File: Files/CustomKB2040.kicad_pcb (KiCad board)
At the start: 2 copper layers, 3.9 x 3.6 mm, 153 parts, among them J1 USB_C_Receptacle, J3 USB_C_Receptacle, J4 USB_C_Receptacle, J5 Conn_01x03_Pin, J6 USB_C_Receptacle, U1 W25Q128JVS, U2 XC6206-3.3_SOT, U3 USBLC6-2SC6, U4 RP2040, U5 W25Q128JVS, U6 XC6206-3.3_SOT, U7 USBLC6-2SC6, U8 RP2040, Y1 Crystal_GND24, Y2 Crystal_GND24

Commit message: placed companets and semi routed
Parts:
- added REF**: MountingHole_2.2mm_M2_DIN965_Pad, MountingHole:MountingHole_2.2mm_M2_DIN965_Pad, F.Cu at (46.3, 103.3)
- added REF**: MountingHole_2.2mm_M2_DIN965_Pad, MountingHole:MountingHole_2.2mm_M2_DIN965_Pad, F.Cu at (40.4, 52.2)
- added REF**: MountingHole_2.2mm_M2_DIN965_Pad, MountingHole:MountingHole_2.2mm_M2_DIN965_Pad, F.Cu at (119.9, 98.6)
- added REF**: MountingHole_2.2mm_M2_DIN965_Pad, MountingHole:MountingHole_2.2mm_M2_DIN965_Pad, F.Cu at (138.0, 45.0)
- added REF**: MountingHole_2.2mm_M2_DIN965_Pad, MountingHole:MountingHole_2.2mm_M2_DIN965_Pad, F.Cu at (120.0, 45.0)
- added REF**: MountingHole_2.2mm_M2_DIN965_Pad, MountingHole:MountingHole_2.2mm_M2_DIN965_Pad, F.Cu at (138.9, 98.6)
- added REF**: MountingHole_2.2mm_M2_DIN965_Pad, MountingHole:MountingHole_2.2mm_M2_DIN965_Pad, F.Cu at (99.8, 61.8)
- BOOT1, D1, D2, F1, J1, J3, RESET1, U1, U2, U3, U4, Y1: moved to F.Cu
- C1, C10, C2, C3, C4, C5, C6: footprint ScottoKeebs_Components:Capacitor_0603 -> Capacitor_SMD:C_0805_2012Metric_Pad1.18x1.45mm_HandSolder; moved to F.Cu
- C11, C13, C14, C15, C16, C17, C18, C19, C20, C21, C22, C23, C24, C25, C27, C28, C29, C31, C32, C33, C34, C35, C36, C7, C9: footprint ScottoKeebs_Components:Capacitor_0603 -> Capacitor_SMD:C_0805_2012Metric_Pad1.18x1.45mm_HandSolder
- C12, C26, C30, C8: footprint ScottoKeebs_Components:Capacitor_0402 -> Capacitor_SMD:C_0805_2012Metric_Pad1.18x1.45mm_HandSolder
- R1, R10, R2, R5, R6, R7, R8, R9: footprint Resistor_SMD:R_0603_1608Metric -> Resistor_SMD:R_0805_2012Metric_Pad1.20x1.40mm_HandSolder; moved to F.Cu
- R11, R12, R13, R14, R15, R16, R17, R18, R19, R20, R3, R4: footprint Resistor_SMD:R_0603_1608Metric -> Resistor_SMD:R_0805_2012Metric_Pad1.20x1.40mm_HandSolder
- moved C26 192.8 mm to (231.0, 108.4)
- moved C30 192.8 mm to (231.0, 110.4)
- moved D3 192.8 mm to (242.5, 101.0)
- moved D37 192.8 mm to (243.8, 21.6)
- moved D38 192.8 mm to (243.8, 26.2)
- moved D39 192.8 mm to (243.8, 30.8)
- moved D4 192.8 mm to (242.5, 105.3)
- moved D40 192.8 mm to (243.8, 35.5)
- moved J5 192.8 mm to (227.8, 93.7)
- moved R15 192.8 mm to (238.4, 74.0)
- moved R16 192.8 mm to (238.4, 76.5)
- moved R17 192.8 mm to (238.4, 79.1)
- moved R18 192.8 mm to (238.4, 81.6)
- moved R19 192.8 mm to (238.4, 84.1)
- moved R20 192.8 mm to (238.4, 86.6)
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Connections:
- R10 pad 1: GPIO25 -> GPIO_19
- U4 pad 24: SWCLK -> unconnected-(U4-SWCLK-Pad24)
- U4 pad 25: SWD -> unconnected-(U4-SWD-Pad25)
- U4 pad 30: L_TX -> GPIO_19
- U4 pad 31: L_RX -> unconnected-(U4-GPIO20-Pad31)
- U4 pad 36: unconnected-(U4-GPIO24-Pad36) -> L_TX
- U4 pad 37: GPIO25 -> L_RX
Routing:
- net +5V: track 0.00 -> 445.7 mm, vias 0 -> 7
- net L_TX: track 0.00 -> 26.1 mm
- net L_RX: track 0.00 -> 25.2 mm
- net QSPI_SD3: track 0.00 -> 14.2 mm, vias 0 -> 1
- net QSPI_SCLK: track 0.00 -> 13.6 mm, vias 0 -> 2
- net +3V3: track 0.00 -> 13.5 mm, vias 0 -> 4
- net QSPI_SD0: track 0.00 -> 12.8 mm, vias 0 -> 2
- net +1V1: track 0.00 -> 9.19 mm, vias 0 -> 2
- net QSPI_SS: track 0.00 -> 7.95 mm
- net QSPI_SD1: track 0.00 -> 7.35 mm
- net QSPI_SD2: track 0.00 -> 6.43 mm
- net Net-(U4-XIN): track 0.00 -> 6.35 mm
- net Net-(U4-XOUT): track 0.00 -> 5.43 mm
- net Net-(U2-VO): track 0.00 -> 4.29 mm
- net Net-(C6-Pad1): track 0.00 -> 4.17 mm
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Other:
- board size 3.9 x 3.6 mm -> 225.2 x 105.2 mm

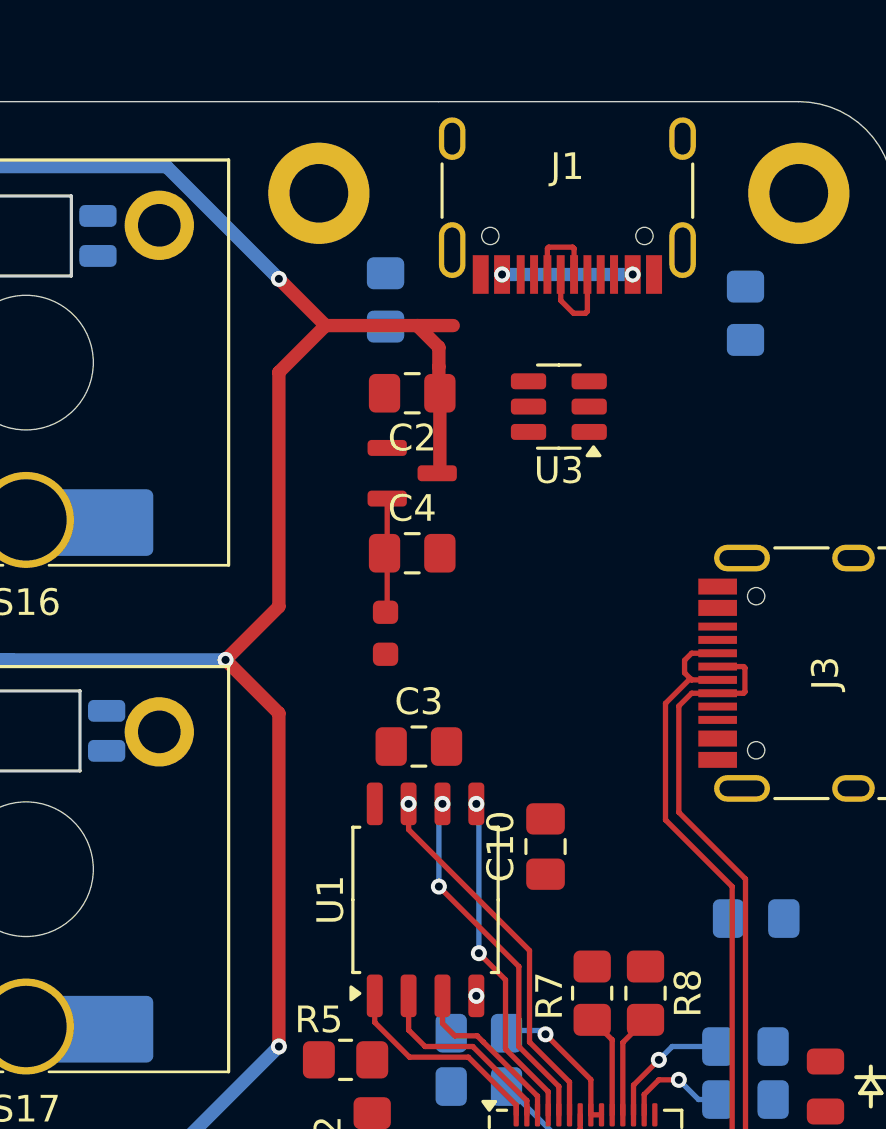
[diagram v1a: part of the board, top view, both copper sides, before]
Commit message: placed companets and semi routed
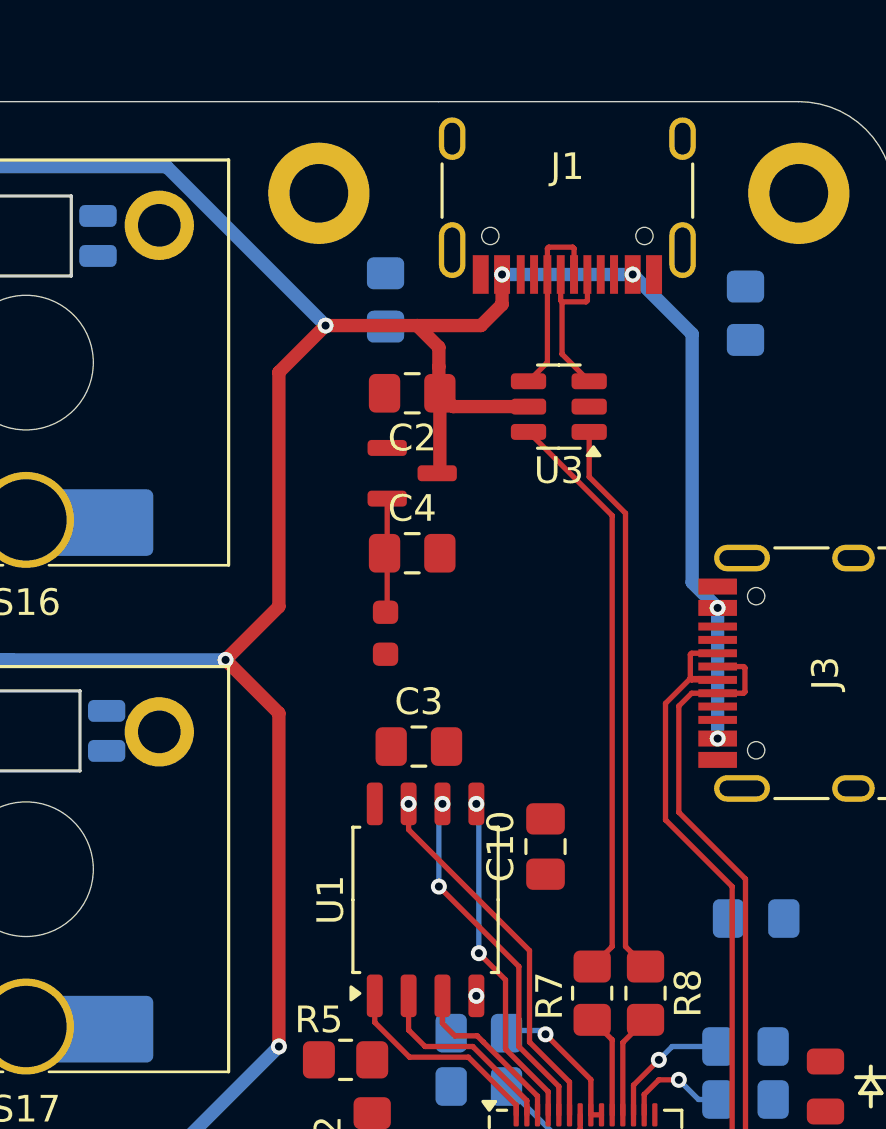
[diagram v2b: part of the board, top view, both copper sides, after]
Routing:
- net +5V: track 445.7 -> 471.2 mm, vias 7 -> 9
- net L_D+: track 0.00 -> 21.7 mm
- net L_D-: track 0.00 -> 20.9 mm
- net USB D+: track 2.99 -> 7.29 mm
- net USB D-: track 3.59 -> 6.39 mm
- net L_RX: track 25.2 -> 26.0 mm

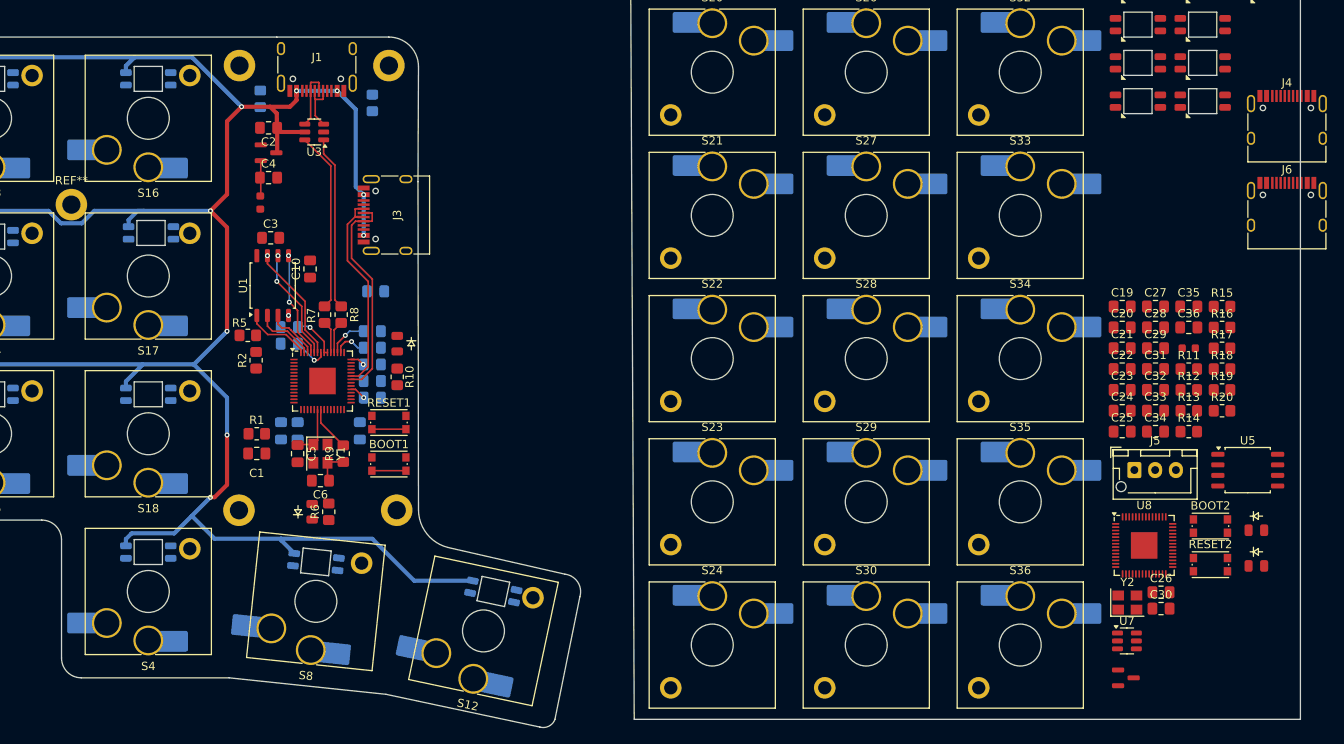
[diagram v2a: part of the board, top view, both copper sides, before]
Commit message: added 5v pads
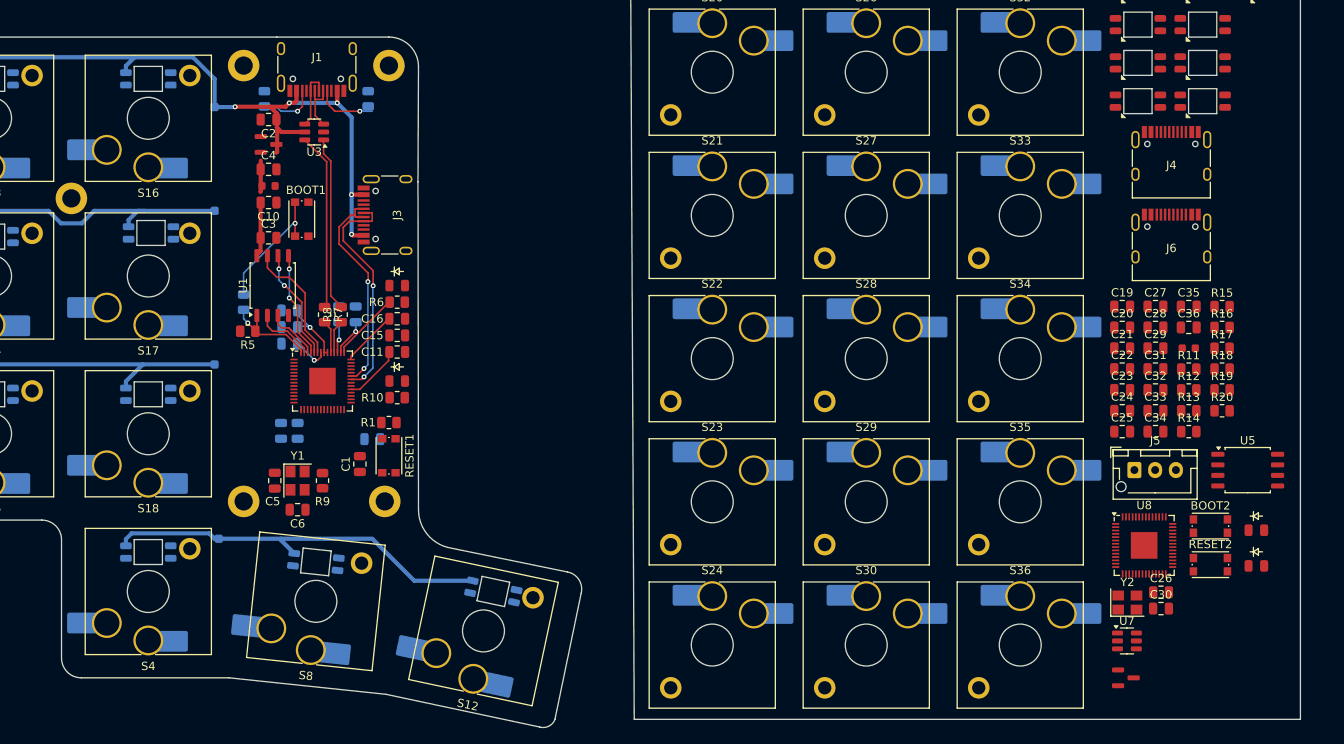
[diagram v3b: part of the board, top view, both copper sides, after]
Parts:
- added REF**: TestPoint_THTPad_1.0x1.0mm_Drill0.5mm, TestPoint:TestPoint_THTPad_1.0x1.0mm_Drill0.5mm, B.Cu at (117.0, 81.0)
- added REF**: TestPoint_THTPad_1.0x1.0mm_Drill0.5mm, TestPoint:TestPoint_THTPad_1.0x1.0mm_Drill0.5mm, B.Cu at (117.0, 50.0)
- added REF**: TestPoint_THTPad_1.0x1.0mm_Drill0.5mm, TestPoint:TestPoint_THTPad_1.0x1.0mm_Drill0.5mm, B.Cu at (117.0, 62.5)
- added REF**: TestPoint_THTPad_1.0x1.0mm_Drill0.5mm, TestPoint:TestPoint_THTPad_1.0x1.0mm_Drill0.5mm, B.Cu at (117.5, 102.0)
- C1, C10, C12, C13, C14, C17, C18, C19, C2, C20, C21, C22, C23, C24, C25, C26, C27, C28, C29, C3, C30, C31, C32, C33, C34, C35, C36, C4, C5, C6, C7, C8, C9: footprint Capacitor_SMD:C_0805_2012Metric_Pad1.18x1.45mm_HandSolder -> Capacitor_SMD:C_0805_2012Metric
- C11, C15, C16: footprint Capacitor_SMD:C_0805_2012Metric_Pad1.18x1.45mm_HandSolder -> Capacitor_SMD:C_0805_2012Metric; moved to F.Cu
- R1, R10, R11, R12, R13, R14, R15, R16, R17, R18, R19, R20, R3, R4, R5, R6, R7, R8, R9: footprint Resistor_SMD:R_0805_2012Metric_Pad1.20x1.40mm_HandSolder -> Resistor_SMD:R_0805_2012Metric
- R2: footprint Resistor_SMD:R_0805_2012Metric_Pad1.20x1.40mm_HandSolder -> Resistor_SMD:R_0805_2012Metric; moved to B.Cu
- moved BOOT1 31.3 mm to (127.5, 63.5), turned to -90 degrees
- moved D1 29.1 mm to (139.0, 71.5), turned to 0 degrees
- moved R6 26.6 mm to (139.0, 73.5), turned to 0 degrees
- moved C9 17.8 mm to (136.0, 90.0)
- moved R1 16.0 mm to (138.0, 88.0)
- moved J4 14.6 mm to (232.2, 57.0)
- moved J6 14.4 mm to (232.2, 67.0)
- moved C16 14.2 mm to (139.0, 75.5), turned to 0 degrees
- moved C17 13.1 mm to (126.0, 74.5), turned to 180 degrees
- moved C1 12.5 mm to (134.5, 93.0), turned to 90 degrees
- moved C10 9.43 mm to (123.5, 61.5), turned to 180 degrees
- moved C15 8.08 mm to (139.0, 77.5)
- moved R2 7.16 mm to (120.5, 73.5), turned to -90 degrees
- moved D2 4.50 mm to (139.0, 83.0), turned to 0 degrees
- moved C12 4.49 mm to (134.0, 75.0), turned to 90 degrees
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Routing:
- net +5V: track 471.2 -> 420.6 mm, vias 9 -> 5
- net +3V3: track 13.5 -> 41.1 mm, vias 4 -> 2
- net USB_BOOT: track 4.10 -> 15.3 mm, vias 0 -> 1
- net Net-(J1-CC2): track 0.00 -> 7.40 mm, vias 0 -> 1
- net Net-(J1-CC1): track 0.00 -> 7.34 mm, vias 0 -> 1
- net Net-(U4-XIN): track 6.35 -> 0.00 mm
- net Net-(U4-XOUT): track 5.43 -> 0.00 mm
- net Net-(C6-Pad1): track 4.17 -> 0.00 mm
- net RESET: track 4.10 -> 0.00 mm
- net QSPI_SS: track 7.95 -> 11.7 mm, vias 0 -> 1
- net L_TX: track 26.1 -> 27.4 mm, vias 0 -> 2
- net +1V1: track 9.19 -> 7.96 mm
- net L_RX: track 26.0 -> 27.2 mm, vias 0 -> 2
- net QSPI_SD3: track 14.2 -> 15.0 mm, vias 1 -> 0
- net Net-(U2-VO): track 4.29 -> 3.79 mm
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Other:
- outline, holes or cut-outs redrawn

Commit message: why is this not working
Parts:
- moved RESET2 0.88 mm to (237.0, 106.0)
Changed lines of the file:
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@@
 	(footprint "Button_Switch_SMD:SW_Push_1P1T_NO_CK_KMR2"
 		(layer "F.Cu")
-		(at 236.96 105.122)
+		(at 236.96 106)
 		(descr "CK components KMR2 tactile switch http://www.ckswitches.com/media/1479/kmr2.pdf")
 		(tags "tactile switch kmr2")

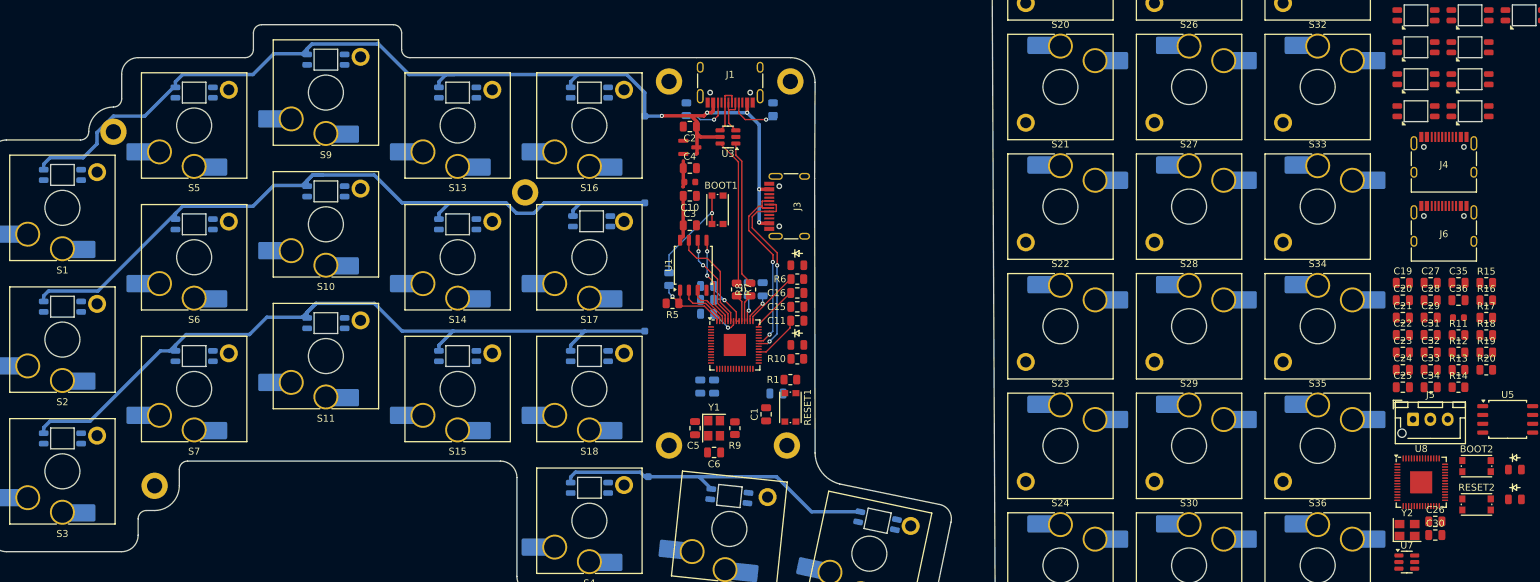
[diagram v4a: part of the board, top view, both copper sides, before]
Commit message: converted to 4 layer board
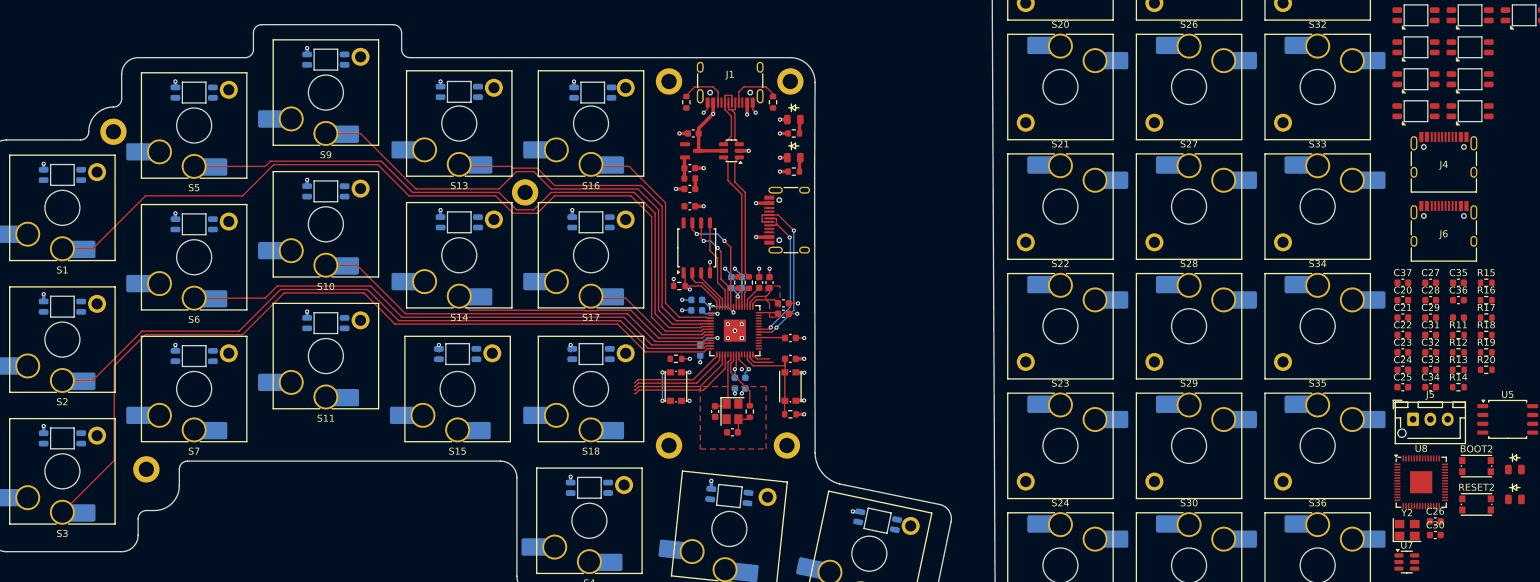
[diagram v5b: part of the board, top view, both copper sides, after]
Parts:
- removed the REF** at (117.0, 81.0)
- removed the REF** at (117.0, 50.0)
- removed the REF** at (117.0, 62.5)
- removed the REF** at (117.5, 102.0)
- added C19: 100n, Capacitor_SMD:C_0603_1608Metric, B.Cu at (125.0, 83.8)
- C1, C10, C11, C13, C14, C15, C16, C17, C18, C2, C20, C21, C22, C23, C24, C25, C26, C27, C28, C29, C3, C30, C31, C32, C33, C34, C35, C36, C4, C5, C6, C7, C9: footprint Capacitor_SMD:C_0805_2012Metric -> Capacitor_SMD:C_0603_1608Metric
- C12, C8: footprint Capacitor_SMD:C_0805_2012Metric -> Capacitor_SMD:C_0603_1608Metric; moved to F.Cu
- C37: renamed from C19; footprint Capacitor_SMD:C_0805_2012Metric -> Capacitor_SMD:C_0603_1608Metric
- R1, R10, R11, R12, R13, R14, R15, R16, R17, R18, R19, R20, R5, R6, R7, R8, R9: footprint Resistor_SMD:R_0805_2012Metric -> Resistor_SMD:R_0603_1608Metric
- R2, R3, R4: footprint Resistor_SMD:R_0805_2012Metric -> Resistor_SMD:R_0603_1608Metric; moved to F.Cu
- moved D2 27.0 mm to (138.5, 56.0)
- moved R10 27.0 mm to (138.5, 58.0)
- moved BOOT1 26.2 mm to (121.5, 89.0)
- moved D1 21.0 mm to (138.5, 50.5)
- moved R6 21.0 mm to (138.5, 52.5)
- moved R2 11.5 mm to (121.5, 85.0), turned to 0 degrees
- moved C18 11.0 mm to (124.5, 78.0), turned to 180 degrees
- moved C1 8.73 mm to (138.0, 85.0), turned to 180 degrees
- moved C11 6.80 mm to (135.0, 74.0), turned to 90 degrees
- moved C17 5.02 mm to (131.0, 74.0), turned to 90 degrees
- moved R1 5.00 mm to (138.0, 93.0), turned to 180 degrees
- moved C9 4.74 mm to (131.5, 88.5), turned to -90 degrees
- moved C15 4.61 mm to (138.0, 82.0)
- moved C14 4.30 mm to (129.5, 74.0), turned to 90 degrees
- moved C6 3.93 mm to (129.7, 95.6)
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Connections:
- net Net-(U2-VO) renamed /Left_Side/3V3_preFuse
- R10 pad 1: GPIO_19 -> GPIO_25
- S1 pad 1: GPIO_1 -> GPIO_5
- S13 pad 1: GPIO_4 -> GPIO_2
- S14 pad 1: GPIO_9 -> GPIO_7
- S16 pad 1: GPIO_5 -> GPIO_1
- S17 pad 1: GPIO_10 -> GPIO_6
- S2 pad 1: GPIO_6 -> GPIO_10
- S5 pad 1: GPIO_2 -> GPIO_4
- S6 pad 1: GPIO_7 -> GPIO_9
- U4 pad 30: GPIO_19 -> unconnected-(U4-GPIO19-Pad30)
- U4 pad 35: unconnected-(U4-GPIO23-Pad35) -> L_RX
- U4 pad 37: L_RX -> GPIO_25
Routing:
- net GPIO_5: track 0.00 -> 119.2 mm
- net GPIO_11: track 0.00 -> 118.3 mm
- net GPIO_10: track 0.00 -> 102.7 mm
- net GPIO_4: track 0.00 -> 95.4 mm
- net GPIO_9: track 0.00 -> 78.9 mm
- net GPIO_3: track 0.00 -> 77.5 mm
- net GPIO_8: track 0.00 -> 60.2 mm
- net GPIO_2: track 0.00 -> 54.3 mm
- net +5V: track 420.6 -> 463.8 mm, vias 5 -> 22
- net GND: track 0.00 -> 39.5 mm, vias 0 -> 35
- net GPIO_7: track 0.00 -> 39.2 mm
- net GPIO_1: track 0.00 -> 35.1 mm
- net GPIO_6: track 0.00 -> 19.9 mm
- net GPIO_15: track 0.00 -> 16.6 mm
- net GPIO_14: track 0.00 -> 15.7 mm
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- added copper zone on F.Cu, net +3V3
- added copper zone on F.Cu, net GND
- added copper zone on In1.Cu, net GND
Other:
- copper layers 2 -> 4
